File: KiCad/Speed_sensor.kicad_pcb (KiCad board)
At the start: 4 copper layers, 35 x 20 mm, 67 parts, among them J1 USB_C_Receptacle_USB2.0, J2 SWD, U1 BQ24040DSQR, U2 OPAMP, U3 ST1PS02, U4 nRF52832-QFxx, U5 LIS2DH12, U6 TP1941U, Y1 32,768kHz, Y2 32MHz

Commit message: Datasheet für quarz hinzugefügt, kleine änderungen am Layout (nichts nennenswertes)
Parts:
- C18, C19: value 12p -> 8p
- moved H10 28.6 mm to (105.3, 32.3)
- moved H11 28.6 mm to (101.4, 32.3)
- moved H9 28.6 mm to (109.1, 32.3)
- moved H1 28.6 mm to (90.0, 32.3)
- moved H12 28.6 mm to (97.6, 32.3)
- moved H3 28.6 mm to (93.8, 32.3)
- moved H4 19.0 mm to (106.7, 62.1)
- moved H5 19.0 mm to (91.2, 62.1)
- moved H7 19.0 mm to (98.8, 62.1)
- moved H6 19.0 mm to (95.0, 62.1)
- moved H8 19.0 mm to (102.8, 62.1)
- moved D1 13.1 mm to (41.8, 30.4)
- moved R1 10.6 mm to (41.8, 34.1), turned to 270 degrees
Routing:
- net Net-(C17-Pad2): track 1.24 -> 3.10 mm
- net GND: track 0.00 -> 1.77 mm
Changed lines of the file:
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@@
     (thickness 1.6)
     (drawings 4)
-    (tracks 5)
+    (tracks 11)
     (zones 0)
     (modules 67)
@@
   )
   (setup
-    (last_trace_width 0.29337)
+    (last_trace_width 0.25)
     (user_trace_width 0.15)
     (user_trace_width 0.2)
@@
       (effects (font (size 1 1) (thickness 0.15)) (justify mirror))
     )
-    (fp_text user %R (at 0 0) (layer B.Fab)
-      (effects (font (size 1 1) (thickness 0.15)) (justify mirror))
-    )
     (fp_line (start 1.705 -3.175) (end -1.705 -3.175) (layer B.Fab) (width 0.1))
     (fp_line (start -1.27 3.175) (end 1.705 3.175) (layer B.Fab) (width 0.1))
@@
     (fp_line (start 4.3 -3.7) (end 4.3 3.7) (layer B.CrtYd) (width 0.05))
     (fp_line (start 4.3 3.7) (end -4.3 3.7) (layer B.CrtYd) (width 0.05))
+    (fp_text user %R (at 0 0) (layer B.Fab)
+      (effects (font (size 1 1) (thickness 0.15)) (justify mirror))
+    )
     (pad 10 smd rect (at 1.95 -2.54 90) (size 2.4 0.74) (layers B.Cu B.Paste B.Mask)
       (net 34 ~RESET~))
@@
     (fp_text value TP1941U (at 0 2 270) (layer F.Fab)
       (effects (font (size 1 1) (thickness 0.15)))
-    )
-    (fp_text user %R (at 0 0) (layer F.Fab)
-      (effects (font (size 0.5 0.5) (thickness 0.075)))
     )
     (fp_line (start 0.7 -1.16) (end -1.2 -1.16) (layer F.SilkS) (width 0.12))
@@
     (fp_line (start 0.675 1.1) (end -0.675 1.1) (layer F.Fab) (width 0.1))
     (fp_line (start -0.175 -1.1) (end -0.675 -0.6) (layer F.Fab) (width 0.1))
+    (fp_text user %R (at 0 0) (layer F.Fab)
+      (effects (font (size 0.5 0.5) (thickness 0.075)))
+    )
     (pad 5 smd rect (at 1.33 -0.65 90) (size 1.5 0.4) (layers F.Cu F.Paste F.Mask)
       (net 64 +BATT))
@@
       (effects (font (size 1 1) (thickness 0.15)))
     )
-    (fp_text value 12p (at 0 1.16) (layer F.Fab) hide
+    (fp_text value 8p (at 0 1.16) (layer F.Fab) hide
       (effects (font (size 1 1) (thickness 0.15)))
     )
@@
       (effects (font (size 1 1) (thickness 0.15)))
     )
-    (fp_text value 12p (at 0 1.16) (layer F.Fab) hide
+    (fp_text value 8p (at 0 1.16) (layer F.Fab) hide
       (effects (font (size 1 1) (thickness 0.15)))
     )
@@
   )
   (module Diode_SMD:D_0603_1608Metric_Pad1.05x0.95mm_HandSolder (layer F.Cu)
-    (at 42.926 43.434 90)
+    (at 41.8 30.4 90)
     (descr "Diode SMD 0603 (1608 Metric), square (rectangular) end terminal, IPC_7351 nominal, (Body size source: http://www.tortai-tech.com/upload/download/2011102023233369053.pdf), generated with kicad-footprint-generator")
     (tags "diode handsolder")
@@
   )
   (module Resistor_SMD:R_0603_1608Metric_Pad0.98x0.95mm_HandSolder (layer F.Cu)
-    (at 45.72 43.942)
+    (at 41.8 34.1 270)
     (descr "Resistor SMD 0603 (1608 Metric), square (rectangular) end terminal, IPC_7351 nominal with elongated pad for handsoldering. (Body size source: IPC-SM-782 page 72, https://www.pcb-3d.com/wordpress/wp-content/uploads/ipc-sm-782a_amendment_1_and_2.pdf), generated with kicad-footprint-generator")
     (tags "resistor handsolder")
     (attr smd)
-    (fp_text reference R1 (at -2.7705 0) (layer F.Fab)
-      (effects (font (size 1 1) (thickness 0.15)))
-    )
-    (fp_text value 200 (at 0 1.43) (layer F.Fab) hide
+    (fp_text reference R1 (at -2.7705 0 90) (layer F.Fab)
+      (effects (font (size 1 1) (thickness 0.15)))
+    )
+    (fp_text value 200 (at 0 1.43 90) (layer F.Fab) hide
       (effects (font (size 1 1) (thickness 0.15)))
     )
@@
     (fp_line (start 1.65 -0.73) (end 1.65 0.73) (layer F.CrtYd) (width 0.05))
     (fp_line (start 1.65 0.73) (end -1.65 0.73) (layer F.CrtYd) (width 0.05))
-    (fp_text user %R (at 0 0) (layer F.Fab)
+    (fp_text user %R (at 0 0 90) (layer F.Fab)
       (effects (font (size 0.4 0.4) (thickness 0.06)))
     )
-    (pad 2 smd roundrect (at 0.9125 0) (size 0.975 0.95) (layers F.Cu F.Paste F.Mask) (roundrect_rratio 0.25)
-      (net 63 GND))
-    (pad 1 smd roundrect (at -0.9125 0) (size 0.975 0.95) (layers F.Cu F.Paste F.Mask) (roundrect_rratio 0.25)
+    (pad 2 smd roundrect (at 0.9125 0 270) (size 0.975 0.95) (layers F.Cu F.Paste F.Mask) (roundrect_rratio 0.25)
+      (net 63 GND))
+    (pad 1 smd roundrect (at -0.9125 0 270) (size 0.975 0.95) (layers F.Cu F.Paste F.Mask) (roundrect_rratio 0.25)
       (net 12 "Net-(D1-Pad1)"))
     (model ${KISYS3DMOD}/Resistor_SMD.3dshapes/R_0603_1608Metric.wrl
@@
   )
   (module TestPoint:TestPoint_Loop_D1.80mm_Drill1.0mm_Beaded (layer F.Cu)
-    (at 105.918 74.2442 180)
+    (at 91.218 62.1442 180)
     (descr "wire loop with bead as test point, loop diameter 1.8mm, hole diameter 1.0mm")
     (tags "test point wire loop bead")
@@
   )
   (module TestPoint:TestPoint_Loop_D1.80mm_Drill1.0mm_Beaded (layer F.Cu)
-    (at 109.728 74.2442 180)
+    (at 95.028 62.1442 180)
     (descr "wire loop with bead as test point, loop diameter 1.8mm, hole diameter 1.0mm")
     (tags "test point wire loop bead")
@@
   )
   (module TestPoint:TestPoint_Loop_D1.80mm_Drill1.0mm_Beaded (layer F.Cu)
-    (at 113.538 74.2442 180)
+    (at 98.838 62.1442 180)
     (descr "wire loop with bead as test point, loop diameter 1.8mm, hole diameter 1.0mm")
     (tags "test point wire loop bead")
@@
   )
   (module TestPoint:TestPoint_Loop_D1.80mm_Drill1.0mm_Beaded (layer F.Cu)
-    (at 117.475 74.2442 180)
+    (at 102.775 62.1442 180)
     (descr "wire loop with bead as test point, loop diameter 1.8mm, hole diameter 1.0mm")
     (tags "test point wire loop bead")
@@
   )
   (module TestPoint:TestPoint_Loop_D1.80mm_Drill1.0mm_Beaded (layer F.Cu)
-    (at 118.618 33.5407)
+    (at 90.018 32.3407)
     (descr "wire loop with bead as test point, loop diameter 1.8mm, hole diameter 1.0mm")
     (tags "test point wire loop bead")
@@
   )
   (module TestPoint:TestPoint_Loop_D1.80mm_Drill1.0mm_Beaded (layer F.Cu)
-    (at 122.428 33.5407)
+    (at 93.828 32.3407)
     (descr "wire loop with bead as test point, loop diameter 1.8mm, hole diameter 1.0mm")
     (tags "test point wire loop bead")
@@
   )
   (module TestPoint:TestPoint_Loop_D1.80mm_Drill1.0mm_Beaded (layer F.Cu)
-    (at 121.412 74.2442 180)
+    (at 106.712 62.1442 180)
     (descr "wire loop with bead as test point, loop diameter 1.8mm, hole diameter 1.0mm")
     (tags "test point wire loop bead")
@@
   )
   (module TestPoint:TestPoint_Loop_D1.80mm_Drill1.0mm_Beaded (layer F.Cu)
-    (at 137.668 33.5026)
+    (at 109.068 32.3026)
     (descr "wire loop with bead as test point, loop diameter 1.8mm, hole diameter 1.0mm")
     (tags "test point wire loop bead")
@@
   )
   (module TestPoint:TestPoint_Loop_D1.80mm_Drill1.0mm_Beaded (layer F.Cu)
-    (at 133.858 33.5026)
+    (at 105.258 32.3026)
     (descr "wire loop with bead as test point, loop diameter 1.8mm, hole diameter 1.0mm")
     (tags "test point wire loop bead")
@@
   )
   (module TestPoint:TestPoint_Loop_D1.80mm_Drill1.0mm_Beaded (layer F.Cu)
-    (at 130.048 33.5026)
+    (at 101.448 32.3026)
     (descr "wire loop with bead as test point, loop diameter 1.8mm, hole diameter 1.0mm")
     (tags "test point wire loop bead")
@@
   )
   (module TestPoint:TestPoint_Loop_D1.80mm_Drill1.0mm_Beaded (layer F.Cu)
-    (at 126.238 33.5026)
+    (at 97.638 32.3026)
     (descr "wire loop with bead as test point, loop diameter 1.8mm, hole diameter 1.0mm")
     (tags "test point wire loop bead")
@@
   (gr_line (start 33.142 36.35) (end 68.142 36.35) (layer Edge.Cuts) (width 0.05))
   (segment (start 61.1775 42.848) (end 62.4195 42.848) (width 0.29337) (layer F.Cu) (net 9))
+  (segment (start 60.7013 44.51284) (end 60.7013 43.7987) (width 0.2) (layer F.Cu) (net 9))
+  (segment (start 61.1775 43.3225) (end 61.1775 42.848) (width 0.2) (layer F.Cu) (net 9))
+  (segment (start 60.7013 43.7987) (end 61.1775 43.3225) (width 0.2) (layer F.Cu) (net 9))
+  (segment (start 60.3013 44.51284) (end 60.3013 43.7013) (width 0.2) (layer F.Cu) (net 63))
+  (segment (start 60.0425 43.4425) (end 60.0425 42.848) (width 0.2) (layer F.Cu) (net 63))
+  (segment (start 60.3013 43.7013) (end 60.0425 43.4425) (width 0.2) (layer F.Cu) (net 63))
   (segment (start 64.172434 42.848) (end 64.749717 42.270717) (width 0.29337) (layer F.Cu) (net 80))
   (segment (start 63.5645 42.848) (end 64.172434 42.848) (width 0.29337) (layer F.Cu) (net 80))

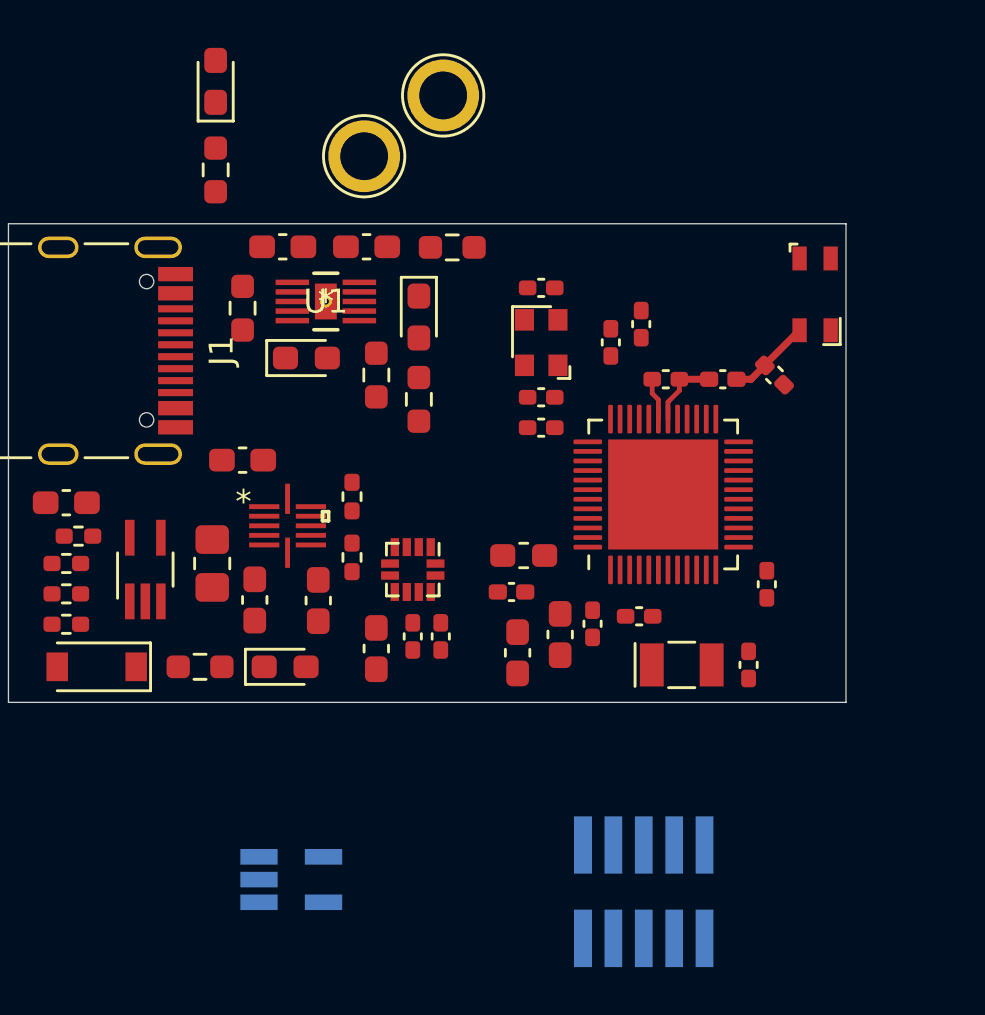
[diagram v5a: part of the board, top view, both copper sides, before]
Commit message: power und GND plane aufgeteilt (quarze noch nicht beachtet, Antenne aber schon)
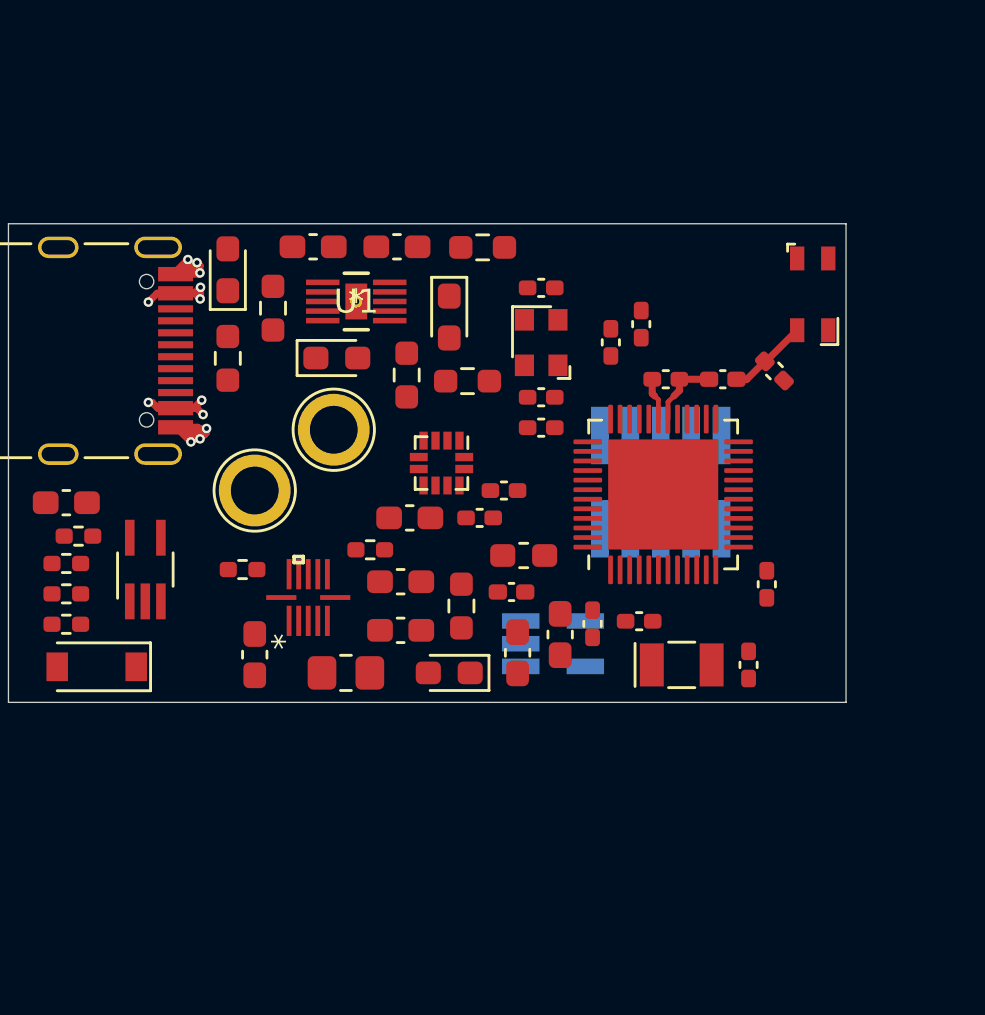
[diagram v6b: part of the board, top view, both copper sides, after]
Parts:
- moved J2 17.1 mm to (60.4, 47.1), turned to 270 degrees
- moved U2 14.7 mm to (55.9, 53.9)
- moved H17 14.7 mm to (43.4, 47.5)
- moved H18 14.7 mm to (46.7, 45.0)
- moved R11 11.2 mm to (52.1, 52.3), turned to 90 degrees
- moved C4 8.14 mm to (43.4, 54.4), turned to 90 degrees
- moved D1 7.89 mm to (42.3, 38.3)
- moved R1 7.89 mm to (42.3, 42.0)
- moved L1 7.22 mm to (47.2, 55.1), turned to 0 degrees
- moved D5 6.86 mm to (51.6, 55.1), turned to 180 degrees
- moved C5 6.64 mm to (53.8, 47.5), turned to 0 degrees
- moved C7 6.23 mm to (49.5, 53.3), turned to 0 degrees
- moved C20 5.69 mm to (52.8, 48.6), turned to 0 degrees
- moved C21 5.64 mm to (49.9, 48.6), turned to 180 degrees
- moved R10 5.49 mm to (42.9, 50.8), turned to 180 degrees
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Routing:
- net GND: track 1.77 -> 13.1 mm, vias 0 -> 6
- net +5V: track 0.00 -> 7.78 mm, vias 0 -> 6
- added copper zone on In2.Cu, net +3V0
- added copper zone on In2.Cu, net +5V
- added copper zone on In2.Cu, net +BATT

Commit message: angefangen mit dem routing
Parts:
- moved C14 3.49 mm to (52.1, 51.7)
- moved R11 2.83 mm to (54.0, 54.4), turned to 270 degrees
- moved R10 0.64 mm to (42.3, 50.8)
- moved C4 0.63 mm to (42.8, 54.4)
- moved C6 0.63 mm to (48.9, 51.3)
- moved C7 0.63 mm to (48.9, 53.3)
- moved L1 0.63 mm to (46.6, 55.1)
- moved R12 0.63 mm to (47.6, 50.0)
- moved U3 0.63 mm to (45.0, 52.0)
- moved D5 0.37 mm to (51.2, 55.2)
- moved L3 0.34 mm to (54.7, 50.5)
- moved L2 0.34 mm to (54.1, 52.1), turned to 180 degrees
- moved C11 0.30 mm to (58.1, 41.1)
- moved C12 0.25 mm to (59.3, 40.5)
- moved C22 0.25 mm to (65.4, 42.5)
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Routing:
- net GND: track 13.1 -> 54.2 mm, vias 6 -> 49
- net +3V0: track 0.00 -> 22.8 mm, vias 0 -> 13
- net Net-(C14-Pad1): track 0.00 -> 8.45 mm
- net +BATT: track 0.00 -> 8.29 mm, vias 0 -> 3
- net Net-(C18-Pad1): track 0.00 -> 7.89 mm
- net +5V: track 7.78 -> 13.7 mm, vias 6 -> 10
- net Net-(C19-Pad1): track 0.00 -> 5.27 mm
- net XL1: track 0.00 -> 4.55 mm
- net BQ_TS: track 0.00 -> 3.74 mm
- net Net-(C12-Pad1): track 0.00 -> 3.64 mm
- net Net-(C11-Pad1): track 0.00 -> 3.39 mm
- net Net-(D5-Pad1): track 0.00 -> 2.63 mm
- net ~BQ_CHG~: track 0.00 -> 2.58 mm
- net Net-(D3-Pad2): track 0.00 -> 2.50 mm
- net BUCK_SW: track 0.00 -> 2.41 mm
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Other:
- net class Default: clearance 0.2 -> 0.127
- rule trace_clearance: 0.2 -> 0.127
